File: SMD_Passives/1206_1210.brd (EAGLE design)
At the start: 10.4 x 3.5 mm, 4 parts

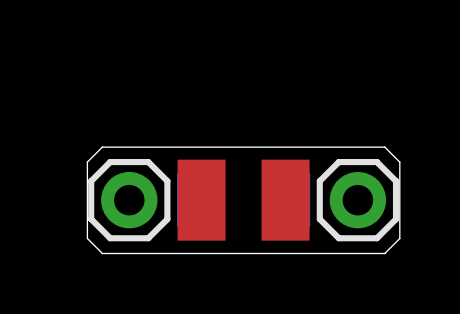
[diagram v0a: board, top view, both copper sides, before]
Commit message: Updated passive SMD breakout boards to meet PCB specs
JLC PCB requires a 5x5mm minimum size, and the single SMD adapters were too small for this, so converted to make them wide enough, and made them "dual" to maximize the spaced used
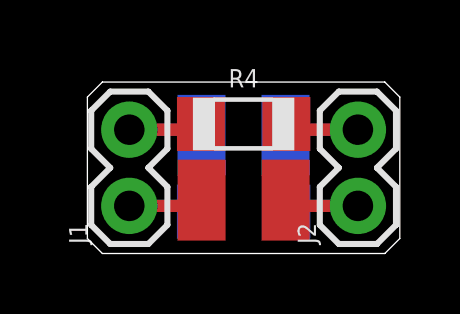
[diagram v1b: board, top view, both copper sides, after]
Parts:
- added R3: (no value), bschulz_passives:R1210
- added R4: (no value), bschulz_passives:R1206
- J1, J2: device bschulz:1X01 -> bschulz:1X02
- moved R2 0.38 mm to (5.21, 1.40)
- moved J1 0.19 mm to (1.40, 1.59), turned to 90 degrees
- moved J2 0.19 mm to (9.02, 1.59), turned to 90 degrees
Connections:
- net N$1 renamed R1_A
- net N$2 renamed R1_B
- new net R2_A: J1.2, R3.1, R4.1
- new net R2_B: J2.2, R3.2, R4.2
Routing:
- net R1_A: track 0.00 -> 4.96 mm
- net R2_B: track 0.00 -> 4.96 mm
- net R2_A: track 0.00 -> 4.96 mm
- net R1_B: track 0.00 -> 4.96 mm
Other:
- board size 10.4 x 3.5 mm -> 10.4 x 5.7 mm
- board text added: "06"
- board text removed: "1206"
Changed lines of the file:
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@@
 <layer number="20" name="Dimension" color="24" fill="1" visible="yes" active="yes"/>
 <layer number="21" name="tPlace" color="7" fill="1" visible="yes" active="yes"/>
-<layer number="22" name="bPlace" color="7" fill="1" visible="yes" active="yes"/>
+<layer number="22" name="bPlace" color="7" fill="1" visible="no" active="yes"/>
 <layer number="23" name="tOrigins" color="15" fill="1" visible="yes" active="yes"/>
-<layer number="24" name="bOrigins" color="15" fill="1" visible="yes" active="yes"/>
+<layer number="24" name="bOrigins" color="15" fill="1" visible="no" active="yes"/>
 <layer number="25" name="tNames" color="7" fill="1" visible="yes" active="yes"/>
-<layer number="26" name="bNames" color="7" fill="1" visible="yes" active="yes"/>
-<layer number="27" name="tValues" color="7" fill="1" visible="yes" active="yes"/>
-<layer number="28" name="bValues" color="7" fill="1" visible="yes" active="yes"/>
+<layer number="26" name="bNames" color="7" fill="1" visible="no" active="yes"/>
+<layer number="27" name="tValues" color="7" fill="1" visible="no" active="yes"/>
+<layer number="28" name="bValues" color="7" fill="1" visible="no" active="yes"/>
 <layer number="29" name="tStop" color="7" fill="3" visible="no" active="yes"/>
 <layer number="30" name="bStop" color="7" fill="6" visible="no" active="yes"/>
@@
 <layer number="38" name="bTest" color="7" fill="1" visible="no" active="yes"/>
 <layer number="39" name="tKeepout" color="4" fill="11" visible="yes" active="yes"/>
-<layer number="40" name="bKeepout" color="1" fill="11" visible="yes" active="yes"/>
+<layer number="40" name="bKeepout" color="1" fill="11" visible="no" active="yes"/>
 <layer number="41" name="tRestrict" color="4" fill="10" visible="yes" active="yes"/>
-<layer number="42" name="bRestrict" color="1" fill="10" visible="yes" active="yes"/>
+<layer number="42" name="bRestrict" color="1" fill="10" visible="no" active="yes"/>
 <layer number="43" name="vRestrict" color="2" fill="10" visible="no" active="yes"/>
-<layer number="44" name="Drills" color="7" fill="1" visible="yes" active="yes"/>
+<layer number="44" name="Drills" color="7" fill="1" visible="no" active="yes"/>
 <layer number="45" name="Holes" color="7" fill="1" visible="yes" active="yes"/>
 <layer number="46" name="Milling" color="3" fill="1" visible="no" active="yes"/>
@@
 <layer number="50" name="dxf" color="7" fill="1" visible="no" active="no"/>
 <layer number="51" name="tDocu" color="7" fill="1" visible="yes" active="yes"/>
-<layer number="52" name="bDocu" color="7" fill="1" visible="yes" active="yes"/>
+<layer number="52" name="bDocu" color="7" fill="1" visible="no" active="yes"/>
 <layer number="53" name="tGND_GNDA" color="7" fill="1" visible="no" active="no"/>
 <layer number="54" name="bGND_GNDA" color="7" fill="1" visible="no" active="no"/>
@@
 <board>
 <plain>
-<wire x1="9.914" y1="3.546" x2="0.5" y2="3.546" width="0" layer="20"/>
-<wire x1="0.5" y1="3.546" x2="0" y2="3.046" width="0" layer="20"/>
-<wire x1="0" y1="3.046" x2="0" y2="0.5" width="0" layer="20"/>
+<wire x1="10.414" y1="0.5" x2="10.414" y2="5.215" width="0" layer="20"/>
+<wire x1="10.414" y1="5.215" x2="9.914" y2="5.715" width="0" layer="20"/>
+<wire x1="9.914" y1="5.715" x2="0.5" y2="5.715" width="0" layer="20"/>
+<wire x1="0.5" y1="5.715" x2="0" y2="5.215" width="0" layer="20"/>
+<wire x1="0" y1="5.215" x2="0" y2="0.5" width="0" layer="20"/>
 <wire x1="0" y1="0.5" x2="0.5" y2="0" width="0" layer="20"/>
 <wire x1="0.5" y1="0" x2="9.914" y2="0" width="0" layer="20"/>
 <wire x1="9.914" y1="0" x2="10.414" y2="0.5" width="0" layer="20"/>
-<wire x1="10.414" y1="0.5" x2="10.414" y2="3.046" width="0" layer="20"/>
-<wire x1="10.414" y1="3.046" x2="9.914" y2="3.546" width="0" layer="20"/>
 <text x="5.207" y="1.778" size="0.6096" layer="51" font="vector" ratio="15" rot="R90" align="center">1210</text>
-<text x="5.207" y="0.381" size="0.6096" layer="52" font="vector" ratio="15" rot="MR180" align="center">1206</text>
+<text x="5.207" y="4.318" size="0.6096" layer="51" font="vector" ratio="15" rot="R90" align="center">06</text>
+<text x="5.207" y="3.937" size="0.6096" layer="52" font="vector" ratio="15" rot="MR90" align="center">1210</text>
+<text x="5.207" y="1.397" size="0.6096" layer="52" font="vector" ratio="15" rot="MR90" align="center">06</text>
 </plain>
 <attributes>
@@
 <attribute name="VALUE" x="2.667" y="-1.397" size="1.27" layer="27"/>
 </element>
-<element name="R2" library="bschulz_passives" package="R1206" value="" x="5.207" y="1.778" smashed="yes" rot="MR180">
-<attribute name="VALUE" x="5.207" y="3.302" size="0.6096" layer="28" font="vector" ratio="15" rot="MR180" align="center"/>
-</element>
-<element name="J1" library="bschulz" package="1X01" package3d_urn="urn:adsk.eagle:package:38028/1" value="" x="1.397" y="1.778" smashed="yes">
-<attribute name="VALUE" x="0.127" y="0.254" size="0.6096" layer="27" font="vector" ratio="20" align="top-left"/>
-</element>
-<element name="J2" library="bschulz" package="1X01" package3d_urn="urn:adsk.eagle:package:38028/1" value="" x="9.017" y="1.778" smashed="yes">
-<attribute name="VALUE" x="7.747" y="0.254" size="0.6096" layer="27" font="vector" ratio="20" align="top-left"/>
+<element name="R2" library="bschulz_passives" package="R1206" value="" x="5.207" y="1.397" smashed="yes" rot="MR180">
+<attribute name="VALUE" x="5.207" y="2.921" size="0.6096" layer="28" font="vector" ratio="15" rot="MR180" align="center"/>
+</element>
+<element name="J1" library="bschulz" package="1X02" value="" x="1.397" y="1.5875" smashed="yes" rot="R90">
+<attribute name="NAME" x="0" y="0.3175" size="0.6096" layer="25" font="vector" ratio="20" rot="R90"/>
+<attribute name="VALUE" x="3.429" y="0.3175" size="0.6096" layer="27" font="vector" ratio="20" rot="R90"/>
+</element>
+<element name="J2" library="bschulz" package="1X02" value="" x="9.017" y="1.5875" smashed="yes" rot="R90">
+<attribute name="NAME" x="7.62" y="0.3175" size="0.6096" layer="25" font="vector" ratio="20" rot="R90"/>
+<attribute name="VALUE" x="11.049" y="0.3175" size="0.6096" layer="27" font="vector" ratio="20" rot="R90"/>
+</element>
+<element name="R3" library="bschulz_passives" package="R1210" value="" x="5.207" y="3.937" smashed="yes" rot="MR180">
+<attribute name="VALUE" x="2.667" y="7.112" size="1.27" layer="28" rot="MR180"/>
+</element>
+<element name="R4" library="bschulz_passives" package="R1206" value="" x="5.207" y="4.318" smashed="yes">
+<attribute name="NAME" x="5.207" y="5.842" size="0.6096" layer="25" font="vector" ratio="15" align="center"/>
+<attribute name="VALUE" x="5.207" y="2.794" size="0.6096" layer="27" font="vector" ratio="15" align="center"/>
 </element>
 </elements>
 <signals>
-<signal name="N$1">
+<signal name="R2_B">
+<contactref element="J2" pad="2"/>
+<contactref element="R4" pad="2"/>
+<contactref element="R3" pad="2"/>
+<wire x1="9.017" y1="4.1275" x2="6.7975" y2="4.1275" width="0.4064" layer="16"/>
+<wire x1="6.7975" y1="4.1275" x2="6.607" y2="3.937" width="0.4064" layer="16"/>
+<wire x1="9.017" y1="4.1275" x2="6.8195" y2="4.1275" width="0.4064" layer="1"/>
+<wire x1="6.8195" y1="4.1275" x2="6.629" y2="4.318" width="0.4064" layer="1"/>
+</signal>
+<signal name="R1_B">
+<contactref element="J2" pad="1"/>
+<contactref element="R2" pad="2"/>
+<contactref element="R1" pad="2"/>
+<wire x1="9.017" y1="1.5875" x2="6.8195" y2="1.5875" width="0.4064" layer="16"/>
+<wire x1="6.8195" y1="1.5875" x2="6.629" y2="1.397" width="0.4064" layer="16"/>
+<wire x1="9.017" y1="1.5875" x2="6.7975" y2="1.5875" width="0.4064" layer="1"/>
+<wire x1="6.7975" y1="1.5875" x2="6.607" y2="1.778" width="0.4064" layer="1"/>
+</signal>
+<signal name="R2_A">
+<contactref element="J1" pad="2"/>
+<contactref element="R3" pad="1"/>
+<contactref element="R4" pad="1"/>
+<wire x1="1.397" y1="4.1275" x2="3.6165" y2="4.1275" width="0.4064" layer="16"/>
+<wire x1="3.6165" y1="4.1275" x2="3.807" y2="3.937" width="0.4064" layer="16"/>
+<wire x1="1.397" y1="4.1275" x2="3.5945" y2="4.1275" width="0.4064" layer="1"/>
+<wire x1="3.5945" y1="4.1275" x2="3.785" y2="4.318" width="0.4064" layer="1"/>
+</signal>
+<signal name="R1_A">
+<contactref element="J1" pad="1"/>
 <contactref element="R1" pad="1"/>
 <contactref element="R2" pad="1"/>
-<contactref element="J1" pad="1"/>
-<wire x1="3.807" y1="1.778" x2="1.397" y2="1.778" width="0" layer="19" extent="1-1"/>
-<wire x1="3.785" y1="1.778" x2="3.807" y2="1.778" width="0" layer="19" extent="1-1"/>
-</signal>
-<signal name="N$2">
-<contactref element="R2" pad="2"/>
-<contactref element="R1" pad="2"/>
-<contactref element="J2" pad="1"/>
-<wire x1="6.607" y1="1.778" x2="9.017" y2="1.778" width="0" layer="19" extent="1-1"/>
-<wire x1="6.629" y1="1.778" x2="6.607" y2="1.778" width="0" layer="19" extent="1-1"/>
+<wire x1="1.397" y1="1.5875" x2="3.5945" y2="1.5875" width="0.4064" layer="16"/>
+<wire x1="3.5945" y1="1.5875" x2="3.785" y2="1.397" width="0.4064" layer="16"/>
+<wire x1="1.397" y1="1.5875" x2="3.6165" y2="1.5875" width="0.4064" layer="1"/>
+<wire x1="3.6165" y1="1.5875" x2="3.807" y2="1.778" width="0.4064" layer="1"/>
 </signal>
 </signals>
@@
 </board>
 </drawing>
-<compatibility>
-<note version="8.3" severity="warning">
-Since Version 8.3, EAGLE supports URNs for individual library
-assets (packages, symbols, and devices). The URNs of those assets
-will not be understood (or retained) with this version.
-</note>
-<note version="8.3" severity="warning">
-Since Version 8.3, EAGLE supports the association of 3D packages
-with devices in libraries, schematics, and board files. Those 3D
-packages will not be understood (or retained) with this version.
-</note>
-</compatibility>
 </eagle>
